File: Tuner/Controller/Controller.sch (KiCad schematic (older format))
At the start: 90 parts, among them J1 Conn_01x06, J10 Conn_01x05, J11 Conn_01x01, J12 Conn_01x02, J14 Conn_01x01, J15 Conn_01x02, J16 Conn_01x06, J17 Conn_01x01, J18 Conn_01x01, J19 Conn_01x01, J2 Conn_01x06, J20 Conn_01x01, J21 Conn_01x01, J22 Conn_01x06, J23 Conn_01x01, J24 Conn_01x01, J25 Conn_01x01, J26 Conn_01x02, J27 Conn_01x02, J28 Conn_01x02, J3 Conn_01x06, J30 Conn_01x02, J4 Conn_01x06, J5 Conn_01x06, J6 Conn_01x06, J7 Conn_01x02, J8 Conn_01x06, J9 Conn_01x06, Q2 2N3904, U4 LM350_TO220

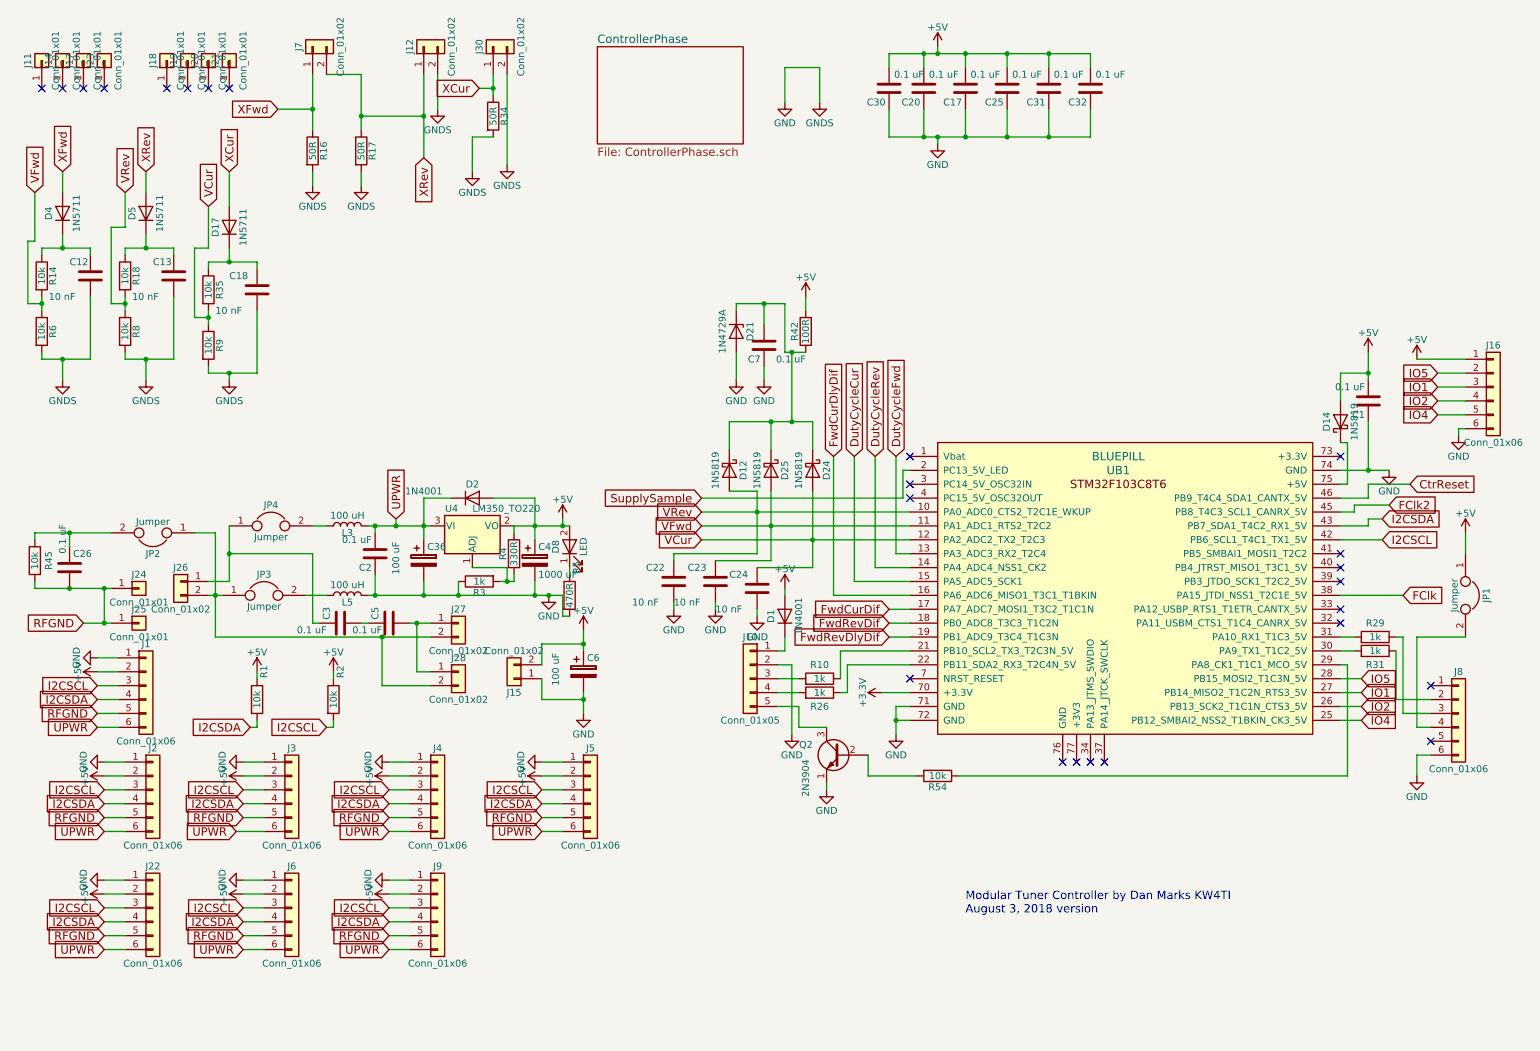
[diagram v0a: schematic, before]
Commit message: JLCPCB order 09232018 - improved grounding - improved I2C cabling - NEO7M port - support for common mode chokes - relay board now has capacitors on all coils
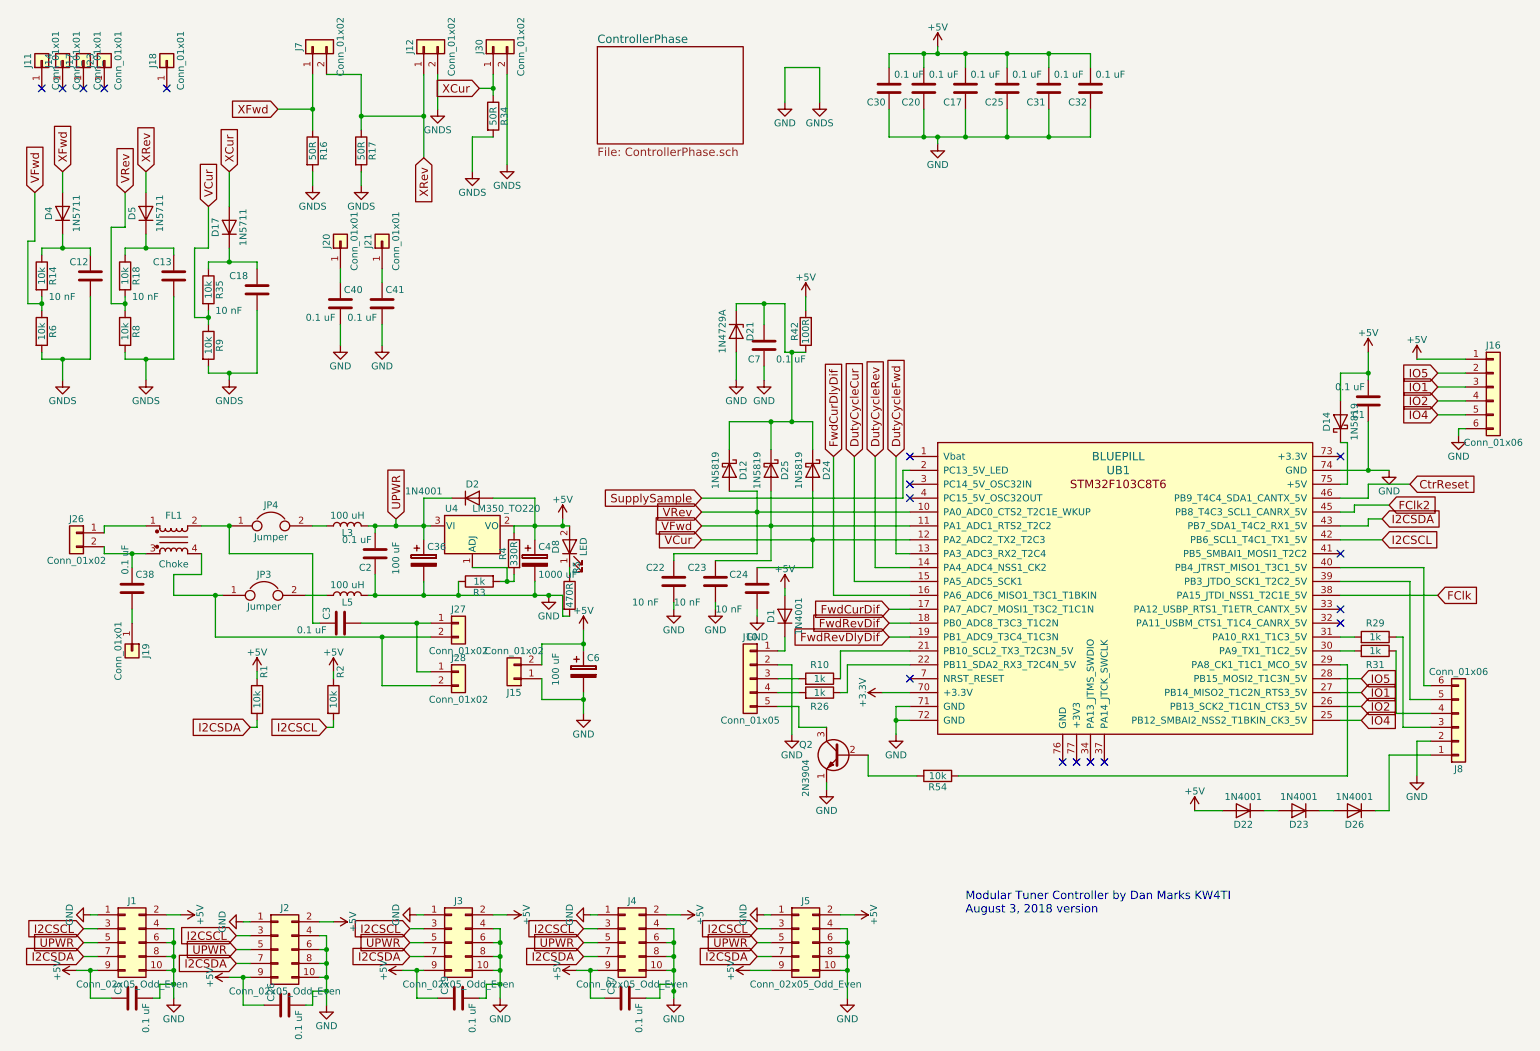
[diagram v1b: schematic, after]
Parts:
- removed J1, J2, J22, J3, J4, J5, J6, J9: Conn_01x06, Connectors_Molex:Molex_KK-6410-06_06x2.54mm_Straight, symbol Conn_01x06
- removed J24, J25: Conn_01x01, Connectors:1pin, symbol Conn_01x01
- removed JP1, JP2: Jumper, Pin_Headers:Pin_Header_Straight_1x02_Pitch2.54mm, symbol Jumper
- removed R45: 10k, Resistors_THT:R_Axial_DIN0207_L6.3mm_D2.5mm_P7.62mm_Horizontal, symbol R
- added C37, C39, C40, C41: 0.1 uF, Capacitors_THT:C_Disc_D5.0mm_W2.5mm_P2.50mm, symbol C
- added C38: 0.1 uF, Capacitors_THT:C_Disc_D10.0mm_W2.5mm_P5.00mm, symbol C
- added D22, D23, D26: 1N4001, Diodes_THT:D_DO-41_SOD81_P7.62mm_Horizontal, symbol D
- added FL1: Choke, Controller:GenericCMCL, symbol EMI_Filter_CommonMode
- added J1, J2, J3, J4, J5: Conn_02x05_Odd_Even, Pin_Headers:Pin_Header_Straight_2x05_Pitch2.54mm, symbol Conn_02x05_Odd_Even
- C26, C5: footprint Capacitors_THT:C_Disc_D12.0mm_W4.4mm_P7.75mm -> Capacitors_THT:C_Disc_D5.0mm_W2.5mm_P2.50mm
- C3: footprint Capacitors_THT:C_Disc_D12.0mm_W4.4mm_P7.75mm -> Capacitors_THT:C_Disc_D10.0mm_W2.5mm_P5.00mm
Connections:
- net RFGND is gone; now on net GND: C26.2
- net +5V: now also C26.1, C5.1, C37.1, C39.1, D22.2 (A), J1.2 (Pin_2), J1.9 (Pin_9), J2.2 (Pin_2), J2.9 (Pin_9), J3.2 (Pin_2), J3.9 (Pin_9), J4.2 (Pin_2), J4.9 (Pin_9), J5.2 (Pin_2), J5.9 (Pin_9)
- net GND: now also C5.2, J8.2 (Pin_2), C37.2, C39.2, C40.2, C41.2, J1.1 (Pin_1), J1.10 (Pin_10), J1.4 (Pin_4), J1.6 (Pin_6), J1.8 (Pin_8), J2.1 (Pin_1), J2.10 (Pin_10), J2.4 (Pin_4), J2.6 (Pin_6), J2.8 (Pin_8), J3.1 (Pin_1), J3.10 (Pin_10), J3.4 (Pin_4), J3.6 (Pin_6), J3.8 (Pin_8), J4.1 (Pin_1), J4.10 (Pin_10), J4.4 (Pin_4), J4.6 (Pin_6), J4.8 (Pin_8), J5.1 (Pin_1), J5.10 (Pin_10), J5.4 (Pin_4), J5.6 (Pin_6), J5.8 (Pin_8); no longer J8.6 (Pin_6)
- net I2CSCL: now also J1.3 (Pin_3), J2.3 (Pin_3), J3.3 (Pin_3), J4.3 (Pin_3), J5.3 (Pin_3)
- net I2CSDA: now also J1.7 (Pin_7), J2.7 (Pin_7), J3.7 (Pin_7), J4.7 (Pin_7), J5.7 (Pin_7)
- net UPWR: now also J1.5 (Pin_5), J2.5 (Pin_5), J3.5 (Pin_5), J4.5 (Pin_5), J5.5 (Pin_5)
- net at J19.1 (Pin_1): now also C38.2
- net at J20.1 (Pin_1): now also C40.1
- net at J21.1 (Pin_1): now also C41.1
- net at C3.2: now also J27.1 (Pin_1), J28.1 (Pin_1); no longer C5.1
- net at J8.1 (Pin_1): now also D26.1 (K)
- net at R31.1: now also J8.4 (Pin_4); no longer J8.2 (Pin_2)
- net at J8.5 (Pin_5): now also UB1.39 (PB3_JTDO_SCK1_T2C2_5V)
- net at UB1.40 (PB4_JTRST_MISO1_T3C1_5V): now also J8.6 (Pin_6)
- net at J27.2 (Pin_2), J28.2 (Pin_2), JP3.1: now also FL1.4; no longer J26.2 (Pin_2)
- net at C3.1, JP4.1: now also FL1.2; no longer J26.1 (Pin_1)
- new net: FL1.1, J26.1 (Pin_1)
- new net: C38.1, FL1.3, J26.2 (Pin_2)
- new net: D22.1 (K), D23.2 (A)
- new net: D23.1 (K), D26.2 (A)
- no-connect marks 24 -> 17
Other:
- moved on the sheet: J19, J20, J21, J26

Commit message: Added boards for SMIH/Schrack Relays
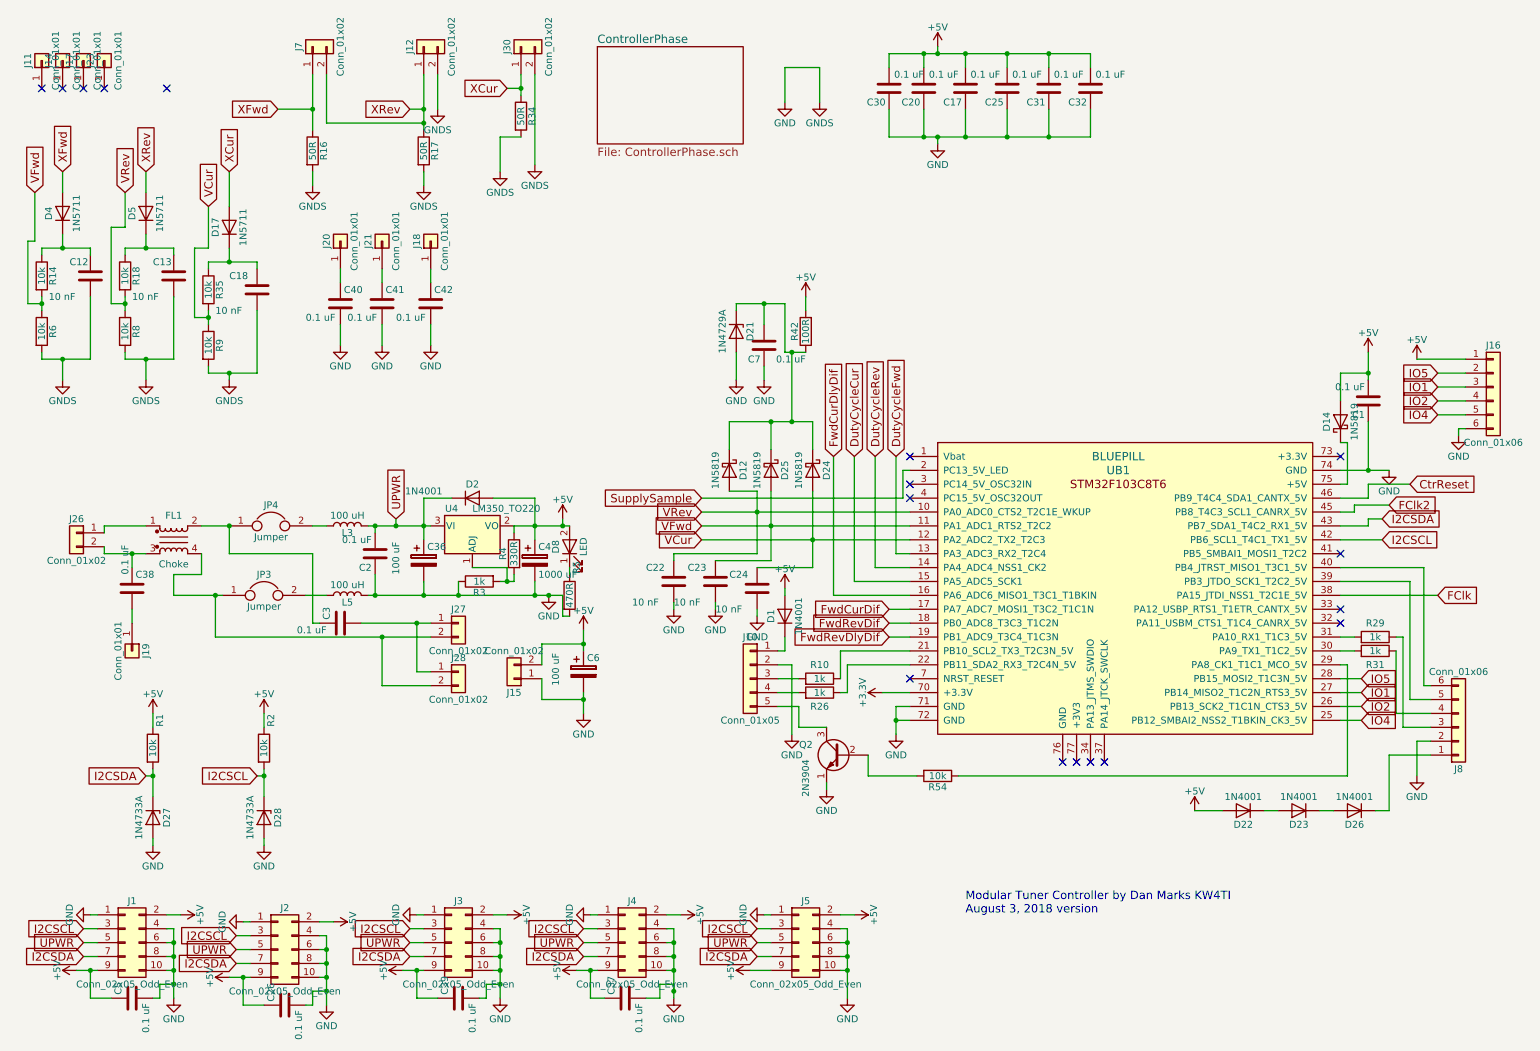
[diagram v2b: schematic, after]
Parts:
- added C42: 0.1 uF, Capacitors_THT:C_Disc_D5.0mm_W2.5mm_P2.50mm, symbol C
- added D27, D28: 1N4733A, Diodes_THT:D_DO-41_SOD81_P7.62mm_Horizontal, symbol D_Zener
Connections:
- net GND: now also C42.2, D27.2 (A), D28.2 (A)
- net I2CSCL: now also D28.1 (K)
- net I2CSDA: now also D27.1 (K)
- net at J18.1 (Pin_1): now also C42.1
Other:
- moved on the sheet: J18, J30, R1, R17, R2, R34

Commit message: Added HK19F boards
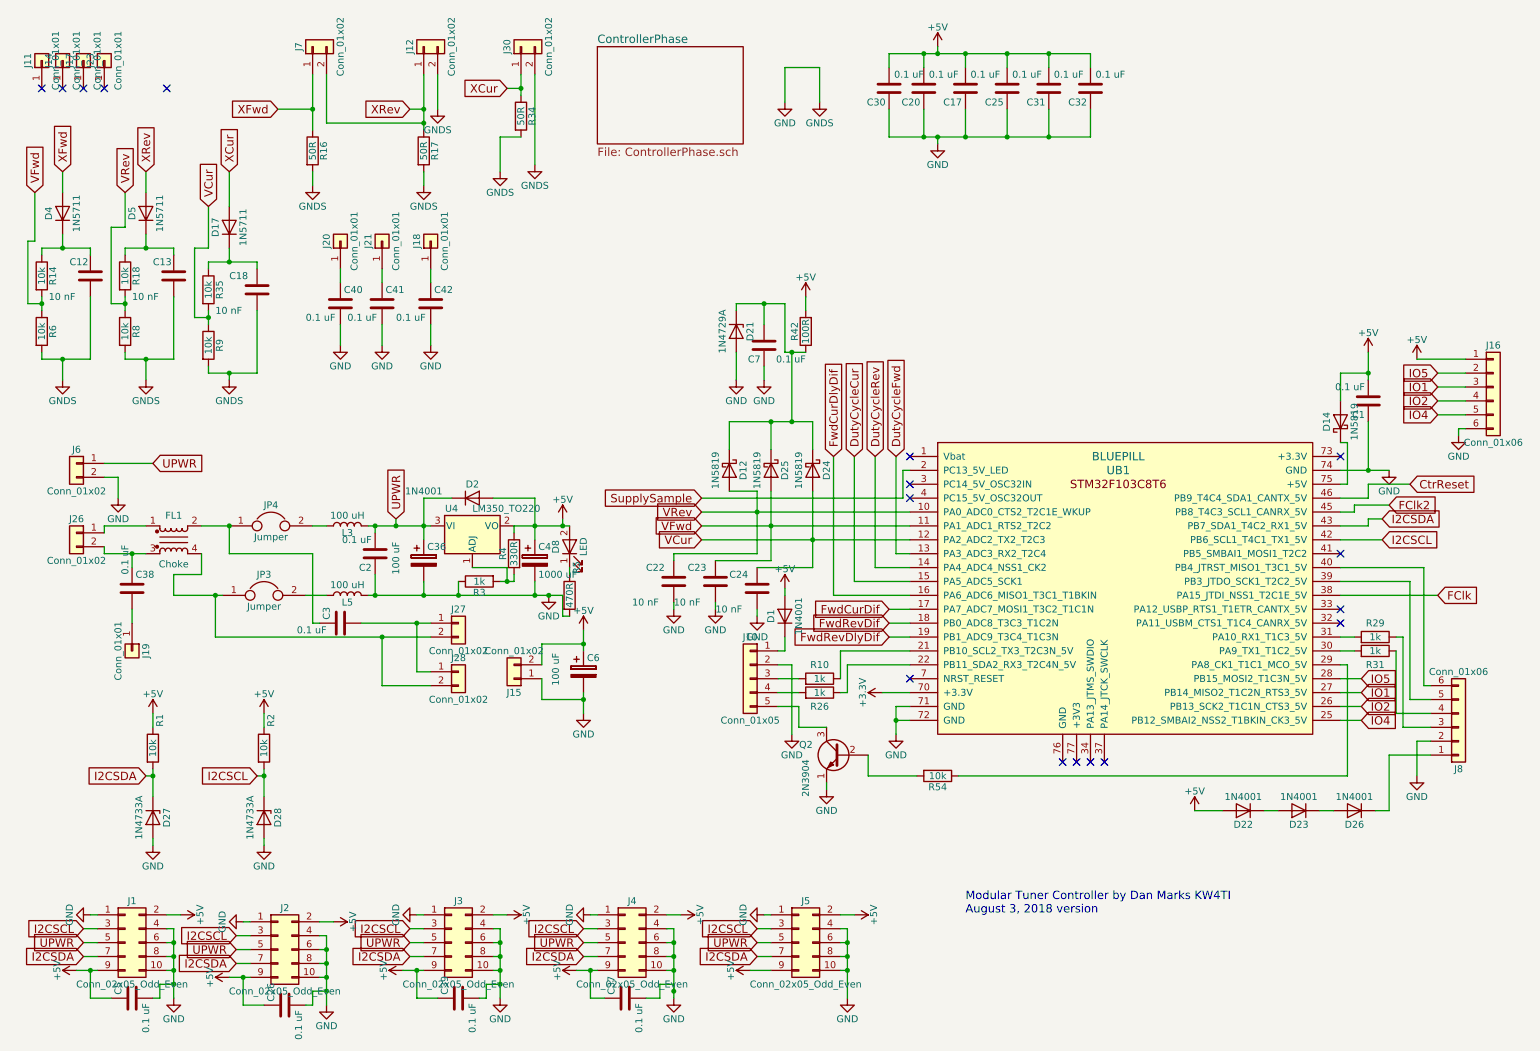
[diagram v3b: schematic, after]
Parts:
- added J6: Conn_01x02, Connectors_Terminal_Blocks:TerminalBlock_bornier-2_P5.08mm, symbol Conn_01x02
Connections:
- net GND: now also J6.2 (Pin_2)
- net UPWR: now also J6.1 (Pin_1)

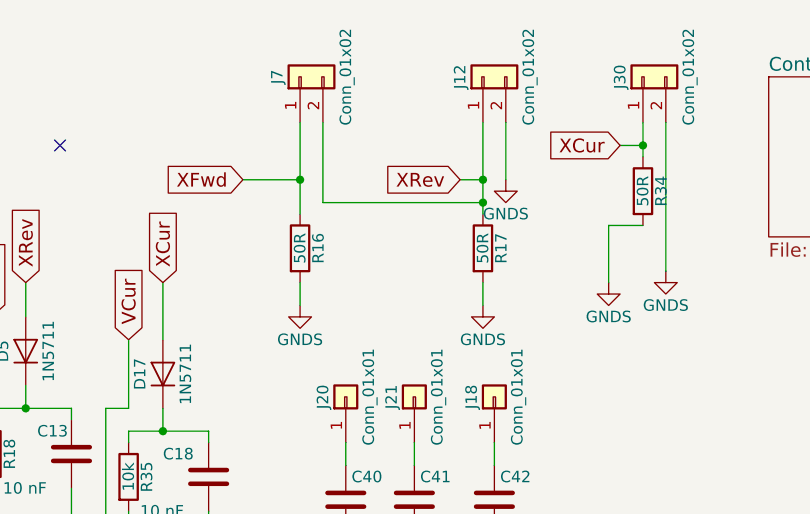
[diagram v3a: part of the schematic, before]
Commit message: Tandem Match PCB added
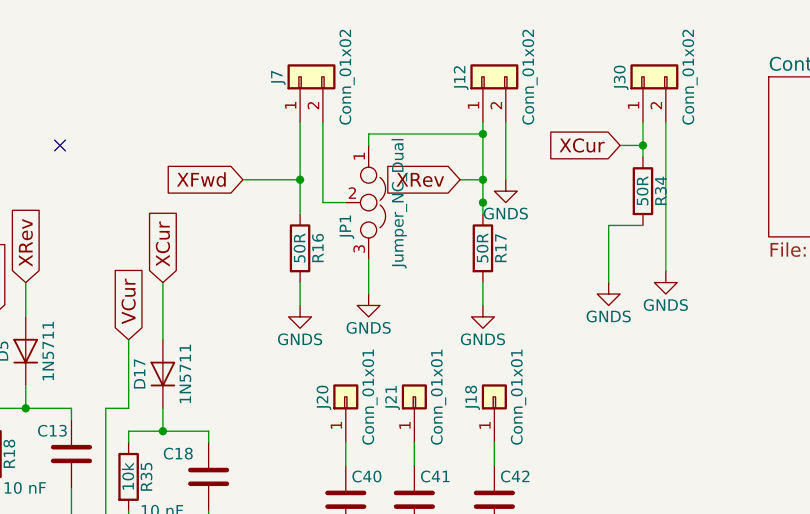
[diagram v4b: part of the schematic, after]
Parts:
- added JP1: Jumper_NC_Dual, Pin_Headers:Pin_Header_Straight_1x03_Pitch2.54mm, symbol Jumper_NC_Dual
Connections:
- net GND: now also JP1.3
- net XRev: now also JP1.1; no longer J7.2 (Pin_2)
- new net: J7.2 (Pin_2), JP1.2

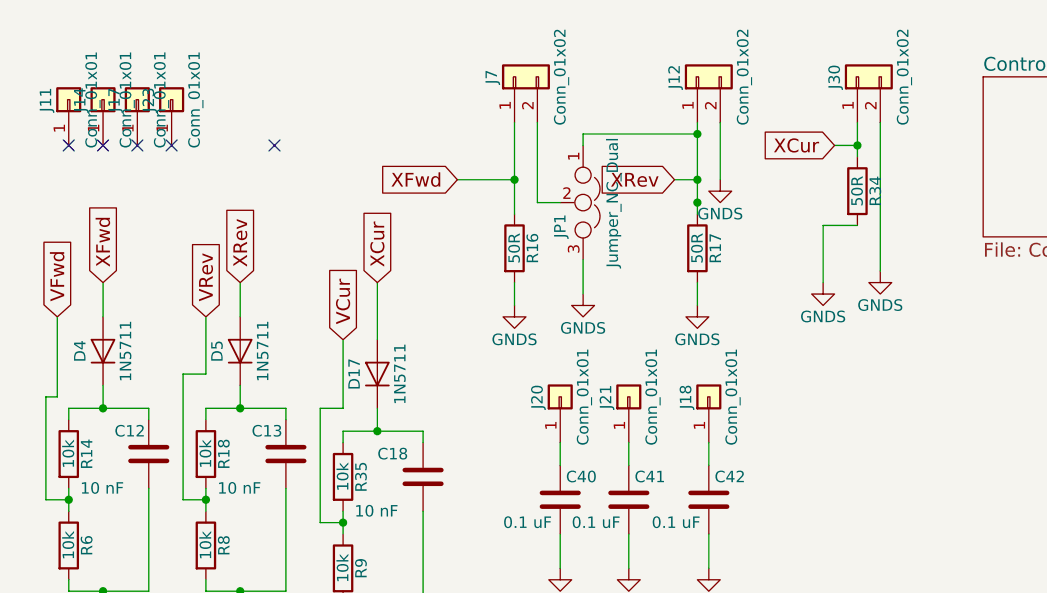
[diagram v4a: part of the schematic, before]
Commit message: Removed 1k resistors, did some more rearranging on TandemMatch
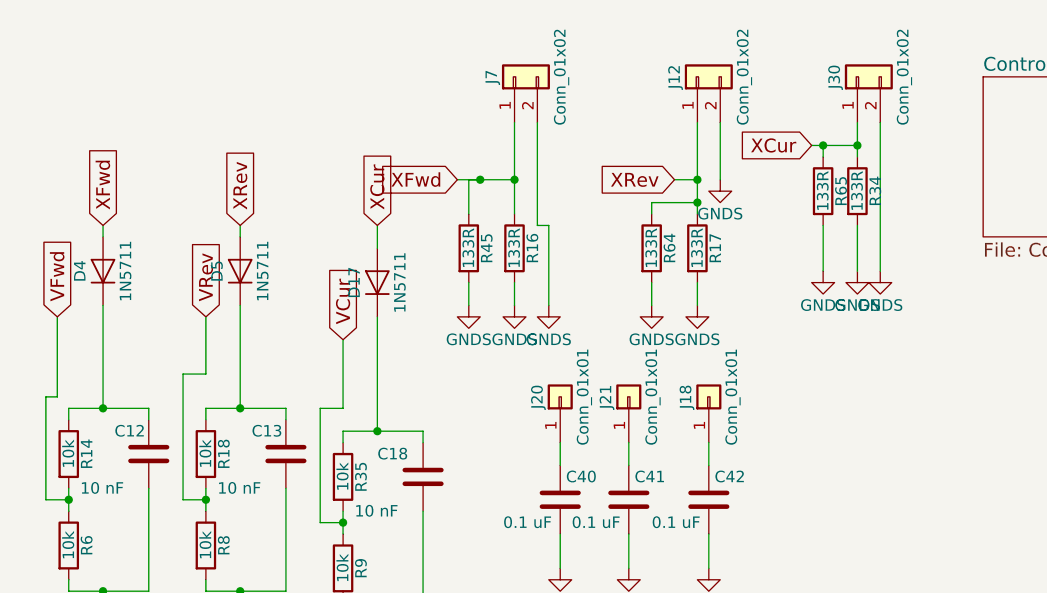
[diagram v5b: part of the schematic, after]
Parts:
- removed J11, J14, J17, J23: Conn_01x01, Connectors:1pin, symbol Conn_01x01
- removed JP1: Jumper_NC_Dual, Pin_Headers:Pin_Header_Straight_1x03_Pitch2.54mm, symbol Jumper_NC_Dual
- added R45, R64, R65: 133R, Resistors_THT:R_Axial_DIN0309_L9.0mm_D3.2mm_P12.70mm_Horizontal, symbol R
- R16, R17, R34: value 50R -> 133R
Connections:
- net GND: now also J7.2 (Pin_2), R45.2, R64.2, R65.2
- net XCur: now also R65.1
- net XFwd: now also R45.1
- net XRev: now also R64.1
- no-connect marks 17 -> 12
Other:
- moved on the sheet: D17, D4, D5
